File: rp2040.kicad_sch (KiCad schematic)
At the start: 30 parts, among them J1 USB_BOOT, J2 USB_C_Receptacle_USB2.0, J3 RESET, U1 W25Q128JVS, U2 XC6206P332MR, U3 RP2040, Y1 12MHz

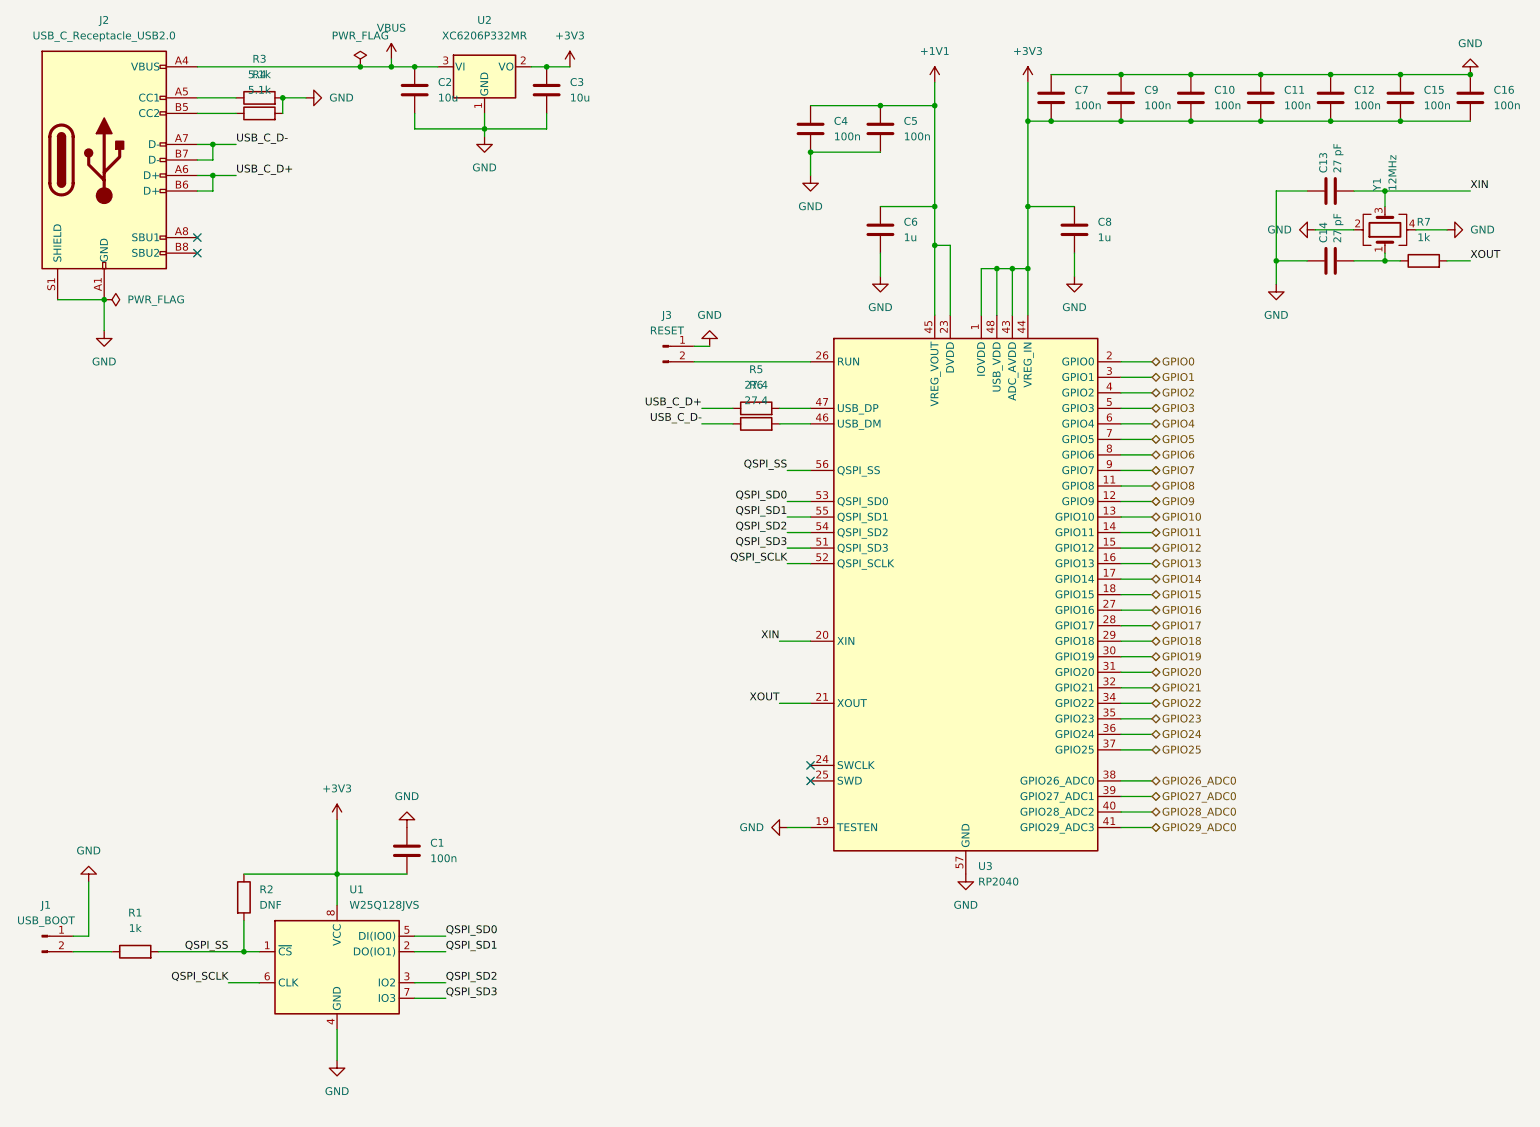
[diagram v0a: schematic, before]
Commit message: Schematic: Update symbols, add esd protection, add I2C header
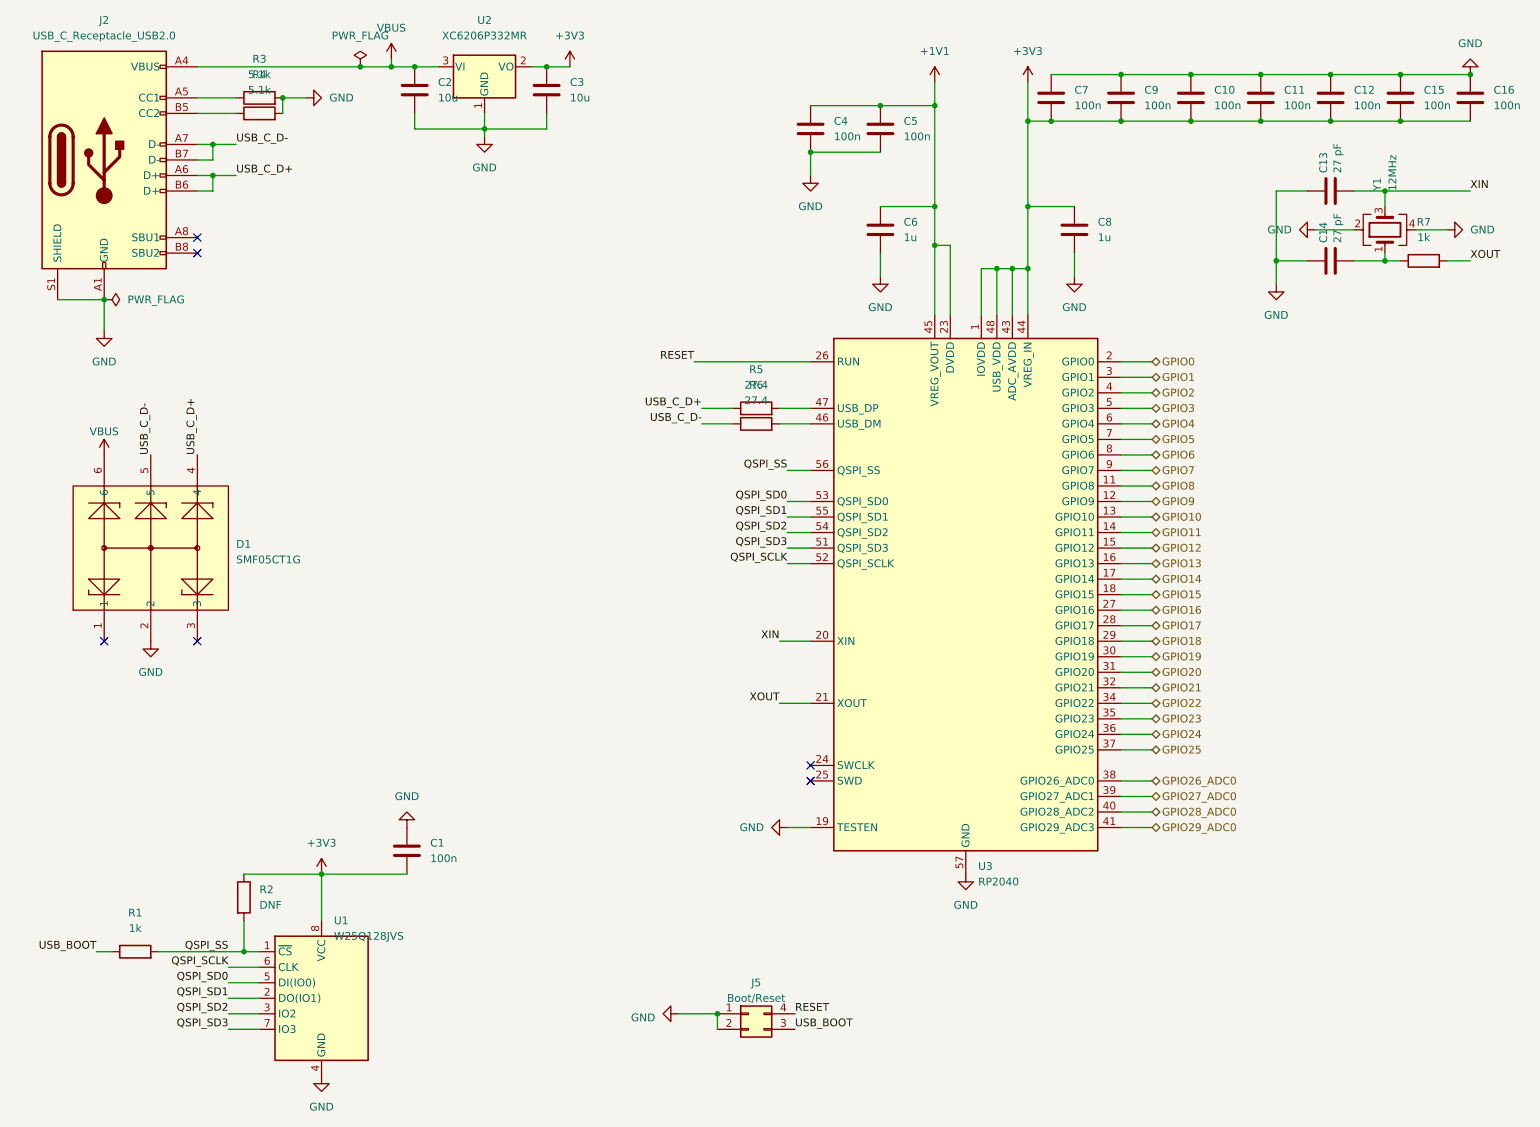
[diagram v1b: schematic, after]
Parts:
- removed J1: USB_BOOT, Connector_PinHeader_2.54mm:PinHeader_1x02_P2.54mm_Vertical, symbol Connector:Conn_01x02_Male
- removed J3: RESET, Connector_PinHeader_2.54mm:PinHeader_1x02_P2.54mm_Vertical, symbol Connector:Conn_01x02_Male
- added D1: SMF05CT1G, esd:SOT-363_L2.0-W1.3-P0.65-LS2.1-BR, symbol easyeda2kicad:SMF05CT1G
- added J5: Boot/Reset, symbol Connector_Generic:Conn_02x02_Counter_Clockwise
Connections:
- net GND: now also D1.2, J5.1 (Pin_1), J5.2 (Pin_2)
- net USB_C_D+: now also D1.4
- net USB_C_D-: now also D1.5
- net VBUS: now also D1.6
- net USB_BOOT: now reaches R1.1
- net USB_BOOT: now also J5.3 (Pin_3)
- net RESET: now reaches U3.26 (RUN)
- net RESET: now also J5.4 (Pin_4)
- no-connect marks 4 -> 6
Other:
- moved on the sheet: U1

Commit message: PCB: Updated new components, removed old paths
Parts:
- J5: footprint (none) -> Connector_PinHeader_2.54mm:PinHeader_2x02_P2.54mm_Vertical
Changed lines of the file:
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@@
       (effects (font (size 1.27 1.27)))
     )
-    (property "Footprint" "" (at 133.35 180.34 0)
+    (property "Footprint" "Connector_PinHeader_2.54mm:PinHeader_2x02_P2.54mm_Vertical" (at 133.35 180.34 0)
       (effects (font (size 1.27 1.27)) hide)
     )

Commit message: JLC: Fixup for JLC Production
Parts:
- R5: value 27.4 -> 27.6; footprint Resistor_SMD:R_0201_0603Metric -> Resistor_SMD:R_1206_3216Metric; LCSC C423620 -> C333003
- R6: footprint Resistor_SMD:R_0201_0603Metric -> Resistor_SMD:R_1206_3216Metric; LCSC C423620 -> C333003
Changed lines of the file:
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@@
       (effects (font (size 1.27 1.27)))
     )
-    (property "Value" "27.4" (at 134.62 77.47 90)
-      (effects (font (size 1.27 1.27)))
-    )
-    (property "Footprint" "Resistor_SMD:R_0201_0603Metric" (at 134.62 83.058 90)
+    (property "Value" "27.6" (at 134.62 77.47 90)
+      (effects (font (size 1.27 1.27)))
+    )
+    (property "Footprint" "Resistor_SMD:R_1206_3216Metric" (at 134.62 83.058 90)
       (effects (font (size 1.27 1.27)) hide)
     )
@@
       (effects (font (size 1.27 1.27)) hide)
     )
-    (property "LCSC" "C423620" (at 134.62 81.28 90)
+    (property "LCSC" "C333003" (at 134.62 81.28 90)
       (effects (font (size 1.27 1.27)) hide)
     )
@@
       (effects (font (size 1.27 1.27)))
     )
-    (property "Footprint" "Resistor_SMD:R_0201_0603Metric" (at 134.62 85.598 90)
+    (property "Footprint" "Resistor_SMD:R_1206_3216Metric" (at 134.62 85.598 90)
       (effects (font (size 1.27 1.27)) hide)
     )
@@
       (effects (font (size 1.27 1.27)) hide)
     )
-    (property "LCSC" "C423620" (at 134.62 83.82 90)
-      (effects (font (size 1.27 1.27)) hide)
-    )
+    (property "LCSC" "C333003" (at 134.62 83.82 90)
+      (effects (font (size 1.27 1.27)) hide)
+    )
